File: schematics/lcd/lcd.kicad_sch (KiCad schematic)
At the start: 18 parts, among them J1 Conn_01x07_Socket, U1 NHD-C12832A1Z, U2 TLV70033_SOT23-5, U3 TXS0104EDR

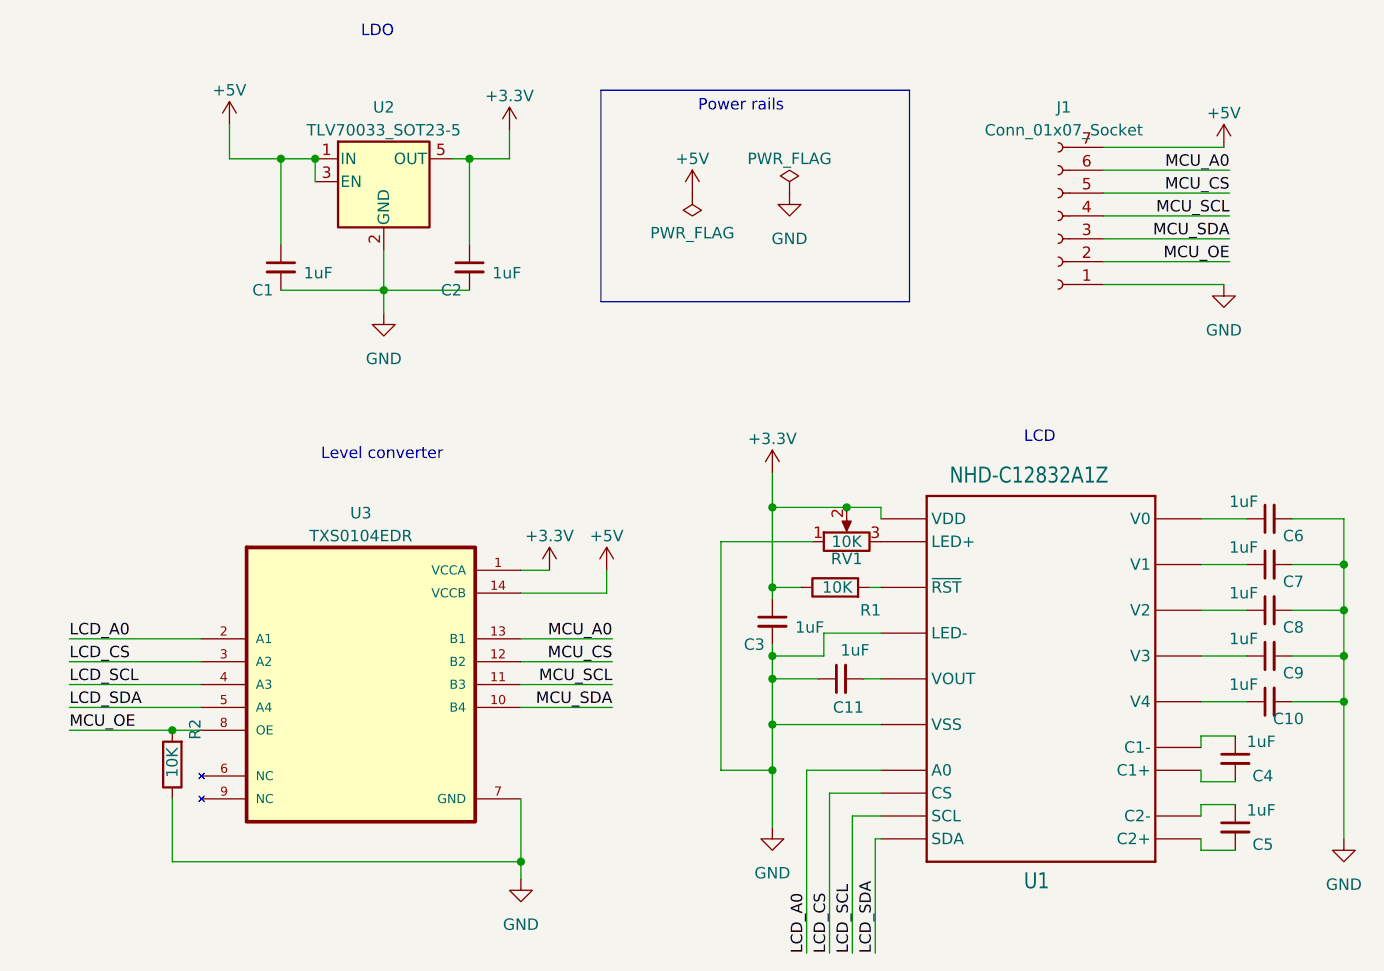
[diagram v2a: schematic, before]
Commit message: SCH: LCD=> fixes, production ready
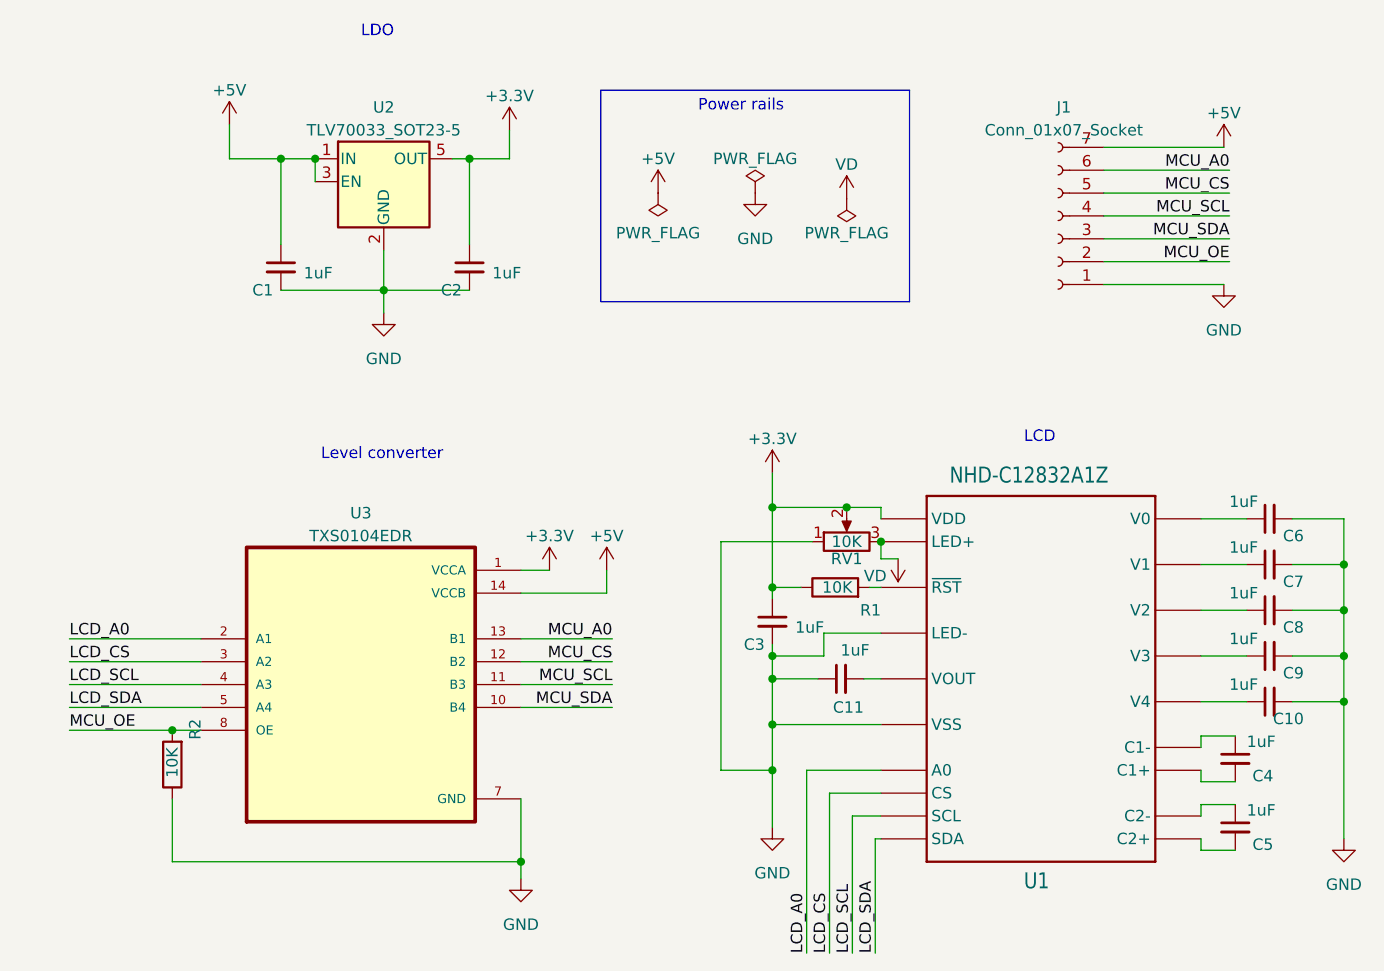
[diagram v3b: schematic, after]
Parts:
- U3: footprint library:SOIC127P600X175-14N -> SOIC127P600X175-14N; LCSC (none) -> C79342
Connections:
- net VD: now reaches RV1.3, U1.P18 (LED+)
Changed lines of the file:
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@@
   (junction (at 143.51 117.475) (diameter 0) (color 0 0 0 0)
   )
+  (junction (at 155.575 104.775) (diameter 0) (color 0 0 0 0)
+  )
   (junction (at 100.33 76.835) (diameter 0) (color 0 0 0 0)
   )
@@
     (stroke (width 0) (type default))
   )
+  (wire (pts (xy 155.575 104.775) (xy 155.575 106.68))
+    (stroke (width 0) (type default))
+  )
   (wire (pts (xy 114.3 62.23) (xy 114.3 59.055))
     (stroke (width 0) (type default))
@@
   )
   (wire (pts (xy 207.01 112.395) (xy 207.01 117.475))
+    (stroke (width 0) (type default))
+  )
+  (wire (pts (xy 155.575 106.68) (xy 157.48 106.68))
     (stroke (width 0) (type default))
   )
@@
     )
   )
-  (symbol (lib_id "power:PWR_FLAG") (at 145.415 66.04 0) (unit 1)
-    (in_bom yes) (on_board yes) (dnp no) (fields_autoplaced)
-    (property "Reference" "#FLG01" (at 145.415 64.135 0)
-      (effects (font (size 1.27 1.27)) hide)
-    )
-    (property "Value" "PWR_FLAG" (at 145.415 62.23 0)
-      (effects (font (size 1.27 1.27)))
-    )
-    (property "Footprint" "" (at 145.415 66.04 0)
-      (effects (font (size 1.27 1.27)) hide)
-    )
-    (property "Datasheet" "~" (at 145.415 66.04 0)
+  (symbol (lib_id "power:PWR_FLAG") (at 141.605 66.04 0) (unit 1)
+    (in_bom yes) (on_board yes) (dnp no) (fields_autoplaced)
+    (property "Reference" "#FLG01" (at 141.605 64.135 0)
+      (effects (font (size 1.27 1.27)) hide)
+    )
+    (property "Value" "PWR_FLAG" (at 141.605 62.23 0)
+      (effects (font (size 1.27 1.27)))
+    )
+    (property "Footprint" "" (at 141.605 66.04 0)
+      (effects (font (size 1.27 1.27)) hide)
+    )
+    (property "Datasheet" "~" (at 141.605 66.04 0)
       (effects (font (size 1.27 1.27)) hide)
     )
@@
     )
   )
-  (symbol (lib_id "power:+5V") (at 134.62 66.04 0) (unit 1)
-    (in_bom yes) (on_board yes) (dnp no) (fields_autoplaced)
-    (property "Reference" "#PWR07" (at 134.62 69.85 0)
-      (effects (font (size 1.27 1.27)) hide)
-    )
-    (property "Value" "+5V" (at 134.62 62.23 0)
-      (effects (font (size 1.27 1.27)))
-    )
-    (property "Footprint" "" (at 134.62 66.04 0)
-      (effects (font (size 1.27 1.27)) hide)
-    )
-    (property "Datasheet" "" (at 134.62 66.04 0)
+  (symbol (lib_id "power:+5V") (at 130.81 66.04 0) (unit 1)
+    (in_bom yes) (on_board yes) (dnp no) (fields_autoplaced)
+    (property "Reference" "#PWR07" (at 130.81 69.85 0)
+      (effects (font (size 1.27 1.27)) hide)
+    )
+    (property "Value" "+5V" (at 130.81 62.23 0)
+      (effects (font (size 1.27 1.27)))
+    )
+    (property "Footprint" "" (at 130.81 66.04 0)
+      (effects (font (size 1.27 1.27)) hide)
+    )
+    (property "Datasheet" "" (at 130.81 66.04 0)
       (effects (font (size 1.27 1.27)) hide)
     )
@@
     )
   )
-  (symbol (lib_id "power:GND") (at 145.415 66.04 0) (unit 1)
-    (in_bom yes) (on_board yes) (dnp no) (fields_autoplaced)
-    (property "Reference" "#PWR09" (at 145.415 72.39 0)
-      (effects (font (size 1.27 1.27)) hide)
-    )
-    (property "Value" "GND" (at 145.415 71.12 0)
-      (effects (font (size 1.27 1.27)))
-    )
-    (property "Footprint" "" (at 145.415 66.04 0)
-      (effects (font (size 1.27 1.27)) hide)
-    )
-    (property "Datasheet" "" (at 145.415 66.04 0)
+  (symbol (lib_id "power:GND") (at 141.605 66.04 0) (unit 1)
+    (in_bom yes) (on_board yes) (dnp no) (fields_autoplaced)
+    (property "Reference" "#PWR09" (at 141.605 72.39 0)
+      (effects (font (size 1.27 1.27)) hide)
+    )
+    (property "Value" "GND" (at 141.605 71.12 0)
+      (effects (font (size 1.27 1.27)))
+    )
+    (property "Footprint" "" (at 141.605 66.04 0)
+      (effects (font (size 1.27 1.27)) hide)
+    )
+    (property "Datasheet" "" (at 141.605 66.04 0)
       (effects (font (size 1.27 1.27)) hide)
     )
@@
     )
   )
+  (symbol (lib_id "power:PWR_FLAG") (at 151.765 66.675 180) (unit 1)
+    (in_bom yes) (on_board yes) (dnp no) (fields_autoplaced)
+    (property "Reference" "#FLG02" (at 151.765 68.58 0)
+      (effects (font (size 1.27 1.27)) hide)
+    )
+    (property "Value" "PWR_FLAG" (at 151.765 70.485 0)
+      (effects (font (size 1.27 1.27)))
+    )
+    (property "Footprint" "" (at 151.765 66.675 0)
+      (effects (font (size 1.27 1.27)) hide)
+    )
+    (property "Datasheet" "~" (at 151.765 66.675 0)
+      (effects (font (size 1.27 1.27)) hide)
+    )
+    (pin "1")
+    (instances
+      (project "lcd"
+        (path "/3da7706e-8391-4331-ba0b-48fd1cd1300f"
+          (reference "#FLG02") (unit 1)
+        )
+      )
+    )
+  )
   (symbol (lib_id "power:GND") (at 193.675 76.2 0) (unit 1)
     (in_bom yes) (on_board yes) (dnp no) (fields_autoplaced)
@@
     )
   )
+  (symbol (lib_id "power:VD") (at 151.765 66.675 0) (unit 1)
+    (in_bom yes) (on_board yes) (dnp no)
+    (property "Reference" "#PWR015" (at 151.765 70.485 0)
+      (effects (font (size 1.27 1.27)) hide)
+    )
+    (property "Value" "VD" (at 151.765 62.865 0)
+      (effects (font (size 1.27 1.27)))
+    )
+    (property "Footprint" "" (at 151.765 66.675 0)
+      (effects (font (size 1.27 1.27)) hide)
+    )
+    (property "Datasheet" "" (at 151.765 66.675 0)
+      (effects (font (size 1.27 1.27)) hide)
+    )
+    (pin "1")
+    (instances
+      (project "lcd"
+        (path "/3da7706e-8391-4331-ba0b-48fd1cd1300f"
+          (reference "#PWR015") (unit 1)
+        )
+      )
+    )
+  )
   (symbol (lib_id "power:+5V") (at 193.675 60.96 0) (unit 1)
     (in_bom yes) (on_board yes) (dnp no) (fields_autoplaced)
@@
     )
   )
+  (symbol (lib_id "power:VD") (at 157.48 106.68 180) (unit 1)
+    (in_bom yes) (on_board yes) (dnp no)
+    (property "Reference" "#PWR014" (at 157.48 102.87 0)
+      (effects (font (size 1.27 1.27)) hide)
+    )
+    (property "Value" "VD" (at 154.94 108.585 0)
+      (effects (font (size 1.27 1.27)))
+    )
+    (property "Footprint" "" (at 157.48 106.68 0)
+      (effects (font (size 1.27 1.27)) hide)
+    )
+    (property "Datasheet" "" (at 157.48 106.68 0)
+      (effects (font (size 1.27 1.27)) hide)
+    )
+    (pin "1")
+    (instances
+      (project "lcd"
+        (path "/3da7706e-8391-4331-ba0b-48fd1cd1300f"
+          (reference "#PWR014") (unit 1)
+        )
+      )
+    )
+  )
   (symbol (lib_id "TXS0104EDR:TXS0104EDR") (at 97.79 120.65 0) (unit 1)
     (in_bom yes) (on_board yes) (dnp no) (fields_autoplaced)
@@
       (effects (font (size 1.27 1.27)))
     )
-    (property "Footprint" "library:SOIC127P600X175-14N" (at 97.79 120.65 0)
+    (property "Footprint" "SOIC127P600X175-14N" (at 97.79 120.65 0)
       (effects (font (size 1.27 1.27)) (justify bottom) hide)
     )
-    (property "Datasheet" "" (at 97.79 120.65 0)
+    (property "Datasheet" "https://datasheet.lcsc.com/lcsc/1811082011_Texas-Instruments-TXS0104EDR_C79342.pdf" (at 97.79 120.65 0)
+      (effects (font (size 1.27 1.27)) hide)
+    )
+    (property "LCSC" "C79342" (at 97.79 120.65 0)
       (effects (font (size 1.27 1.27)) hide)
     )
@@
     (pin "7")
     (pin "8")
-    (pin "6")
-    (pin "9")
     (instances
       (project "lcd"
@@
     )
   )
-  (symbol (lib_id "power:PWR_FLAG") (at 134.62 66.04 180) (unit 1)
-    (in_bom yes) (on_board yes) (dnp no) (fields_autoplaced)
-    (property "Reference" "#FLG03" (at 134.62 67.945 0)
-      (effects (font (size 1.27 1.27)) hide)
-    )
-    (property "Value" "PWR_FLAG" (at 134.62 70.485 0)
-      (effects (font (size 1.27 1.27)))
-    )
-    (property "Footprint" "" (at 134.62 66.04 0)
-      (effects (font (size 1.27 1.27)) hide)
-    )
-    (property "Datasheet" "~" (at 134.62 66.04 0)
-      (effects (font (size 1.27 1.27)) hide)
-    )
+  (symbol (lib_id "power:PWR_FLAG") (at 130.81 66.04 180) (unit 1)
+    (in_bom yes) (on_board yes) (dnp no) (fields_autoplaced)
+    (property "Reference" "#FLG03" (at 130.81 67.945 0)
+      (effects (font (size 1.27 1.27)) hide)
+    )
+    (property "Value" "PWR_FLAG" (at 130.81 70.485 0)
+      (effects (font (size 1.27 1.27)))
+    )
+    (property "Footprint" "" (at 130.81 66.04 0)
+      (effects (font (size 1.27 1.27)) hide)
+    )
+    (property "Datasheet" "~" (at 130.81 66.04 0)
+      (effects (font (size 1.27 1.27)) hide)
+    )

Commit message: SCH: LCD => removed MB OE connection, now pulled to 3.3, always ON
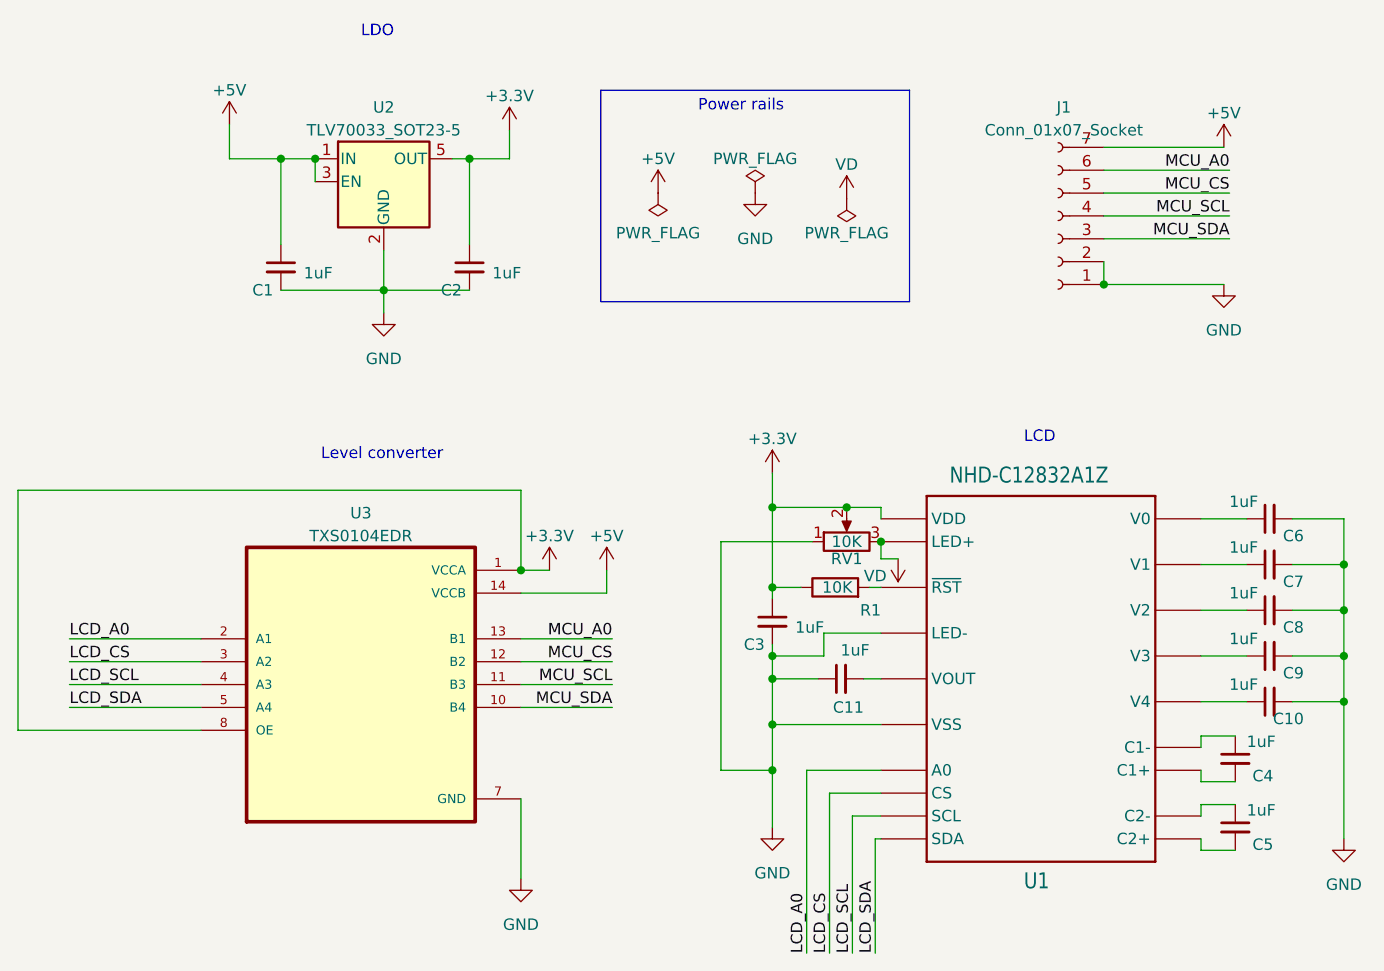
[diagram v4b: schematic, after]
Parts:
- removed R2: 10K, Resistor_SMD:R_0603_1608Metric, symbol Device:R
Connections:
- net +3.3V: now also U3.8 (OE)
- net GND: now also J1.2 (Pin_2)
- removed net MCU_OE: J1.2 (Pin_2), U3.8 (OE)
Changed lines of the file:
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@@
 (kicad_sch (version 20230121) (generator eeschema)
   (paper "A4")
-  (junction (at 76.835 125.73) (diameter 0) (color 0 0 0 0)
-  )
   (junction (at 143.51 125.095) (diameter 0) (color 0 0 0 0)
   )
   (junction (at 109.855 62.23) (diameter 0) (color 0 0 0 0)
   )
+  (junction (at 115.57 107.95) (diameter 0) (color 0 0 0 0)
+  )
   (junction (at 207.01 122.555) (diameter 0) (color 0 0 0 0)
   )
@@
   (junction (at 207.01 107.315) (diameter 0) (color 0 0 0 0)
   )
+  (junction (at 180.34 76.2) (diameter 0) (color 0 0 0 0)
+  )
   (junction (at 92.71 62.23) (diameter 0) (color 0 0 0 0)
   )
@@
   (junction (at 143.51 100.965) (diameter 0) (color 0 0 0 0)
   )
-  (junction (at 115.57 140.335) (diameter 0) (color 0 0 0 0)
-  )
   (junction (at 143.51 109.855) (diameter 0) (color 0 0 0 0)
   )
@@
     (stroke (width 0) (type default))
   )
+  (wire (pts (xy 180.34 73.66) (xy 180.34 76.2))
+    (stroke (width 0) (type default))
+  )
   (wire (pts (xy 154.305 109.855) (xy 155.575 109.855))
     (stroke (width 0) (type default))
@@
     (stroke (width 0) (type default))
   )
-  (wire (pts (xy 115.57 133.35) (xy 115.57 140.335))
+  (wire (pts (xy 115.57 133.35) (xy 115.57 142.24))
     (stroke (width 0) (type default))
   )
@@
     (stroke (width 0) (type default))
   )
-  (wire (pts (xy 76.835 125.73) (xy 80.01 125.73))
-    (stroke (width 0) (type default))
-  )
   (wire (pts (xy 154.94 137.795) (xy 154.94 150.495))
     (stroke (width 0) (type default))
@@
     (stroke (width 0) (type default))
   )
+  (wire (pts (xy 59.69 99.06) (xy 115.57 99.06))
+    (stroke (width 0) (type default))
+  )
   (wire (pts (xy 92.71 62.23) (xy 92.71 64.77))
     (stroke (width 0) (type default))
@@
     (stroke (width 0) (type default))
   )
+  (wire (pts (xy 80.01 125.73) (xy 59.69 125.73))
+    (stroke (width 0) (type default))
+  )
   (wire (pts (xy 151.765 100.965) (xy 143.51 100.965))
     (stroke (width 0) (type default))
@@
     (stroke (width 0) (type default))
   )
-  (wire (pts (xy 76.835 140.335) (xy 115.57 140.335))
-    (stroke (width 0) (type default))
-  )
   (wire (pts (xy 143.51 125.095) (xy 155.575 125.095))
     (stroke (width 0) (type default))
@@
     (stroke (width 0) (type default))
   )
+  (wire (pts (xy 59.69 125.73) (xy 59.69 99.06))
+    (stroke (width 0) (type default))
+  )
   (wire (pts (xy 137.795 104.775) (xy 137.795 130.175))
     (stroke (width 0) (type default))
@@
     (stroke (width 0) (type default))
   )
+  (wire (pts (xy 115.57 99.06) (xy 115.57 107.95))
+    (stroke (width 0) (type default))
+  )
   (wire (pts (xy 191.135 126.365) (xy 191.135 127.635))
     (stroke (width 0) (type default))
@@
     (stroke (width 0) (type default))
   )
-  (wire (pts (xy 76.835 133.35) (xy 76.835 140.335))
-    (stroke (width 0) (type default))
-  )
   (wire (pts (xy 155.575 137.795) (xy 154.94 137.795))
     (stroke (width 0) (type default))
   )
-  (wire (pts (xy 65.405 125.73) (xy 76.835 125.73))
-    (stroke (width 0) (type default))
-  )
   (wire (pts (xy 180.34 60.96) (xy 193.675 60.96))
     (stroke (width 0) (type default))
@@
     (stroke (width 0) (type default))
   )
-  (wire (pts (xy 180.34 73.66) (xy 194.31 73.66))
-    (stroke (width 0) (type default))
-  )
   (wire (pts (xy 180.34 63.5) (xy 194.31 63.5))
-    (stroke (width 0) (type default))
-  )
-  (wire (pts (xy 115.57 142.24) (xy 115.57 140.335))
     (stroke (width 0) (type default))
   )
@@
   (label "MCU_CS" (at 194.31 66.04 180) (fields_autoplaced)
     (effects (font (size 1.27 1.27)) (justify right bottom))
-  )
-  (label "MCU_OE" (at 194.31 73.66 180) (fields_autoplaced)
-    (effects (font (size 1.27 1.27)) (justify right bottom))
-  )
-  (label "MCU_OE" (at 65.405 125.73 0) (fields_autoplaced)
-    (effects (font (size 1.27 1.27)) (justify left bottom))
   )
   (label "MCU_CS" (at 125.73 118.11 180) (fields_autoplaced)
@@
         )
       )
-    )
-  )
-  (symbol (lib_id "Device:R") (at 76.835 129.54 180) (unit 1)
-    (in_bom yes) (on_board yes) (dnp no)
-    (property "Reference" "R2" (at 79.375 124.46 90)
-      (effects (font (size 1.27 1.27)) (justify left))
-    )
-    (property "Value" "10K" (at 76.835 127.635 90)
-      (effects (font (size 1.27 1.27)) (justify left))
-    )
-    (property "Footprint" "Resistor_SMD:R_0603_1608Metric" (at 78.613 129.54 90)
-      (effects (font (size 1.27 1.27)) hide)
-    )
-    (property "Datasheet" "~" (at 76.835 129.54 0)
-      (effects (font (size 1.27 1.27)) hide)
-    )
-    (property "lcsc" "C25804" (at 76.835 129.54 0)
-      (effects (font (size 1.27 1.27)) hide)
-    )
-    (pin "1")
-    (pin "2")
-    (instances
-      (project "lcd"
-        (path "/3da7706e-8391-4331-ba0b-48fd1cd1300f"
-          (reference "R2") (unit 1)
-        )
-      )
